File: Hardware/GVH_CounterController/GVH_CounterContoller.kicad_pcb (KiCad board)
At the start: 2 copper layers, 82.5 x 88.9 mm, 67 parts, among them J1 Molex Micro-Fit 5pos, J10 Molex Micro-Fit 2pos, J11 Molex Micro-Fit 3pos, J2 Conn_02x08_Odd_Even, J3 Molex Ultra-Fit, J6 Molex Micro-Fit 5pos, J7 WIZnet_J1B1211CCD_RJ45, J8 Molex Micro-Fit 2pos, J9 Molex Micro-Fit 2pos, K1 Relay_DPDT, Q1 MBT2222, SW2 SW_DIP_x02, SW3 SW_MEC_5G, U10 AO4882, U11 DS18B20_, U2 SN74LVC2T45, U3 Teensy4.1, U4 R-78E5.0-1.0, U5 SN74LVC2T45DCUR, U6 RT9080-3.3, U7 SN74LVC2T45DCUR, U8 SN74LVC2T45DCUR, U9 SN74LVC2G17

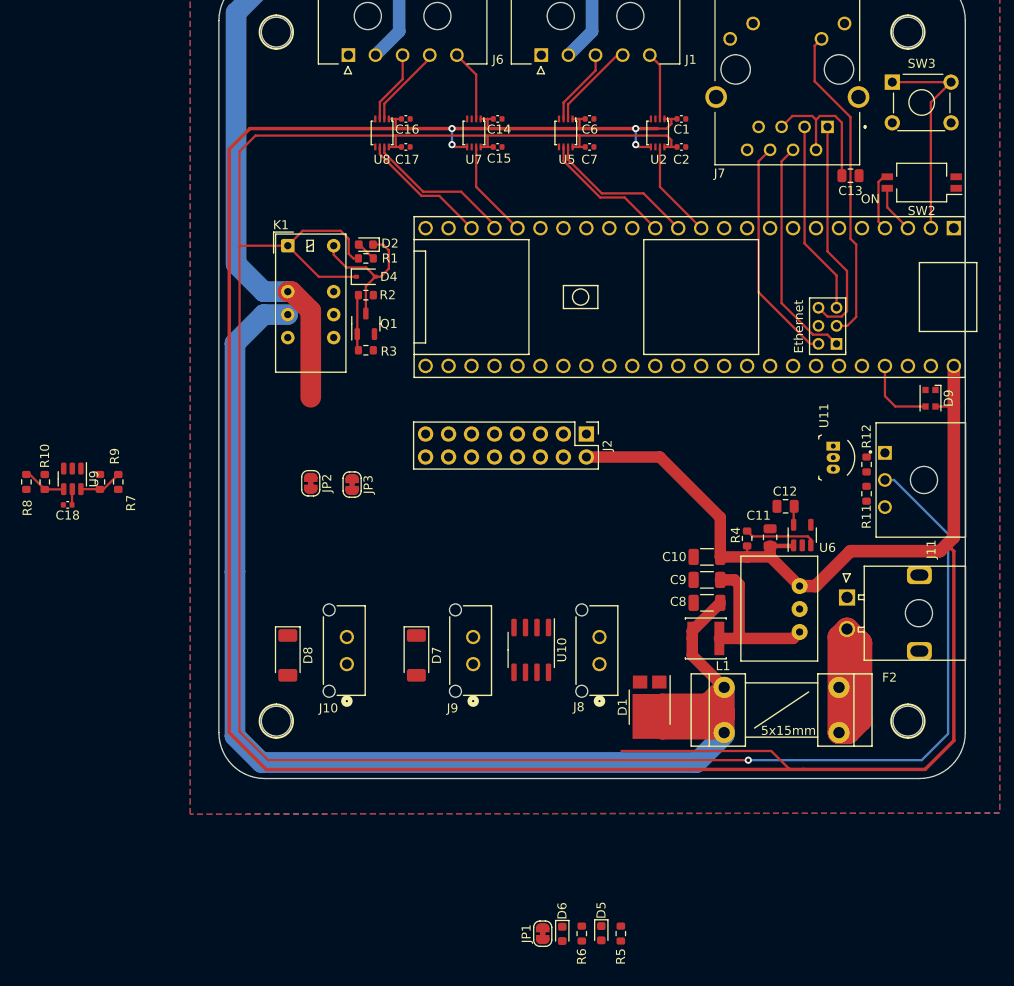
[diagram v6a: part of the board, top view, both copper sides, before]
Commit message: About to change gate driver buffer, it wont shift logic up
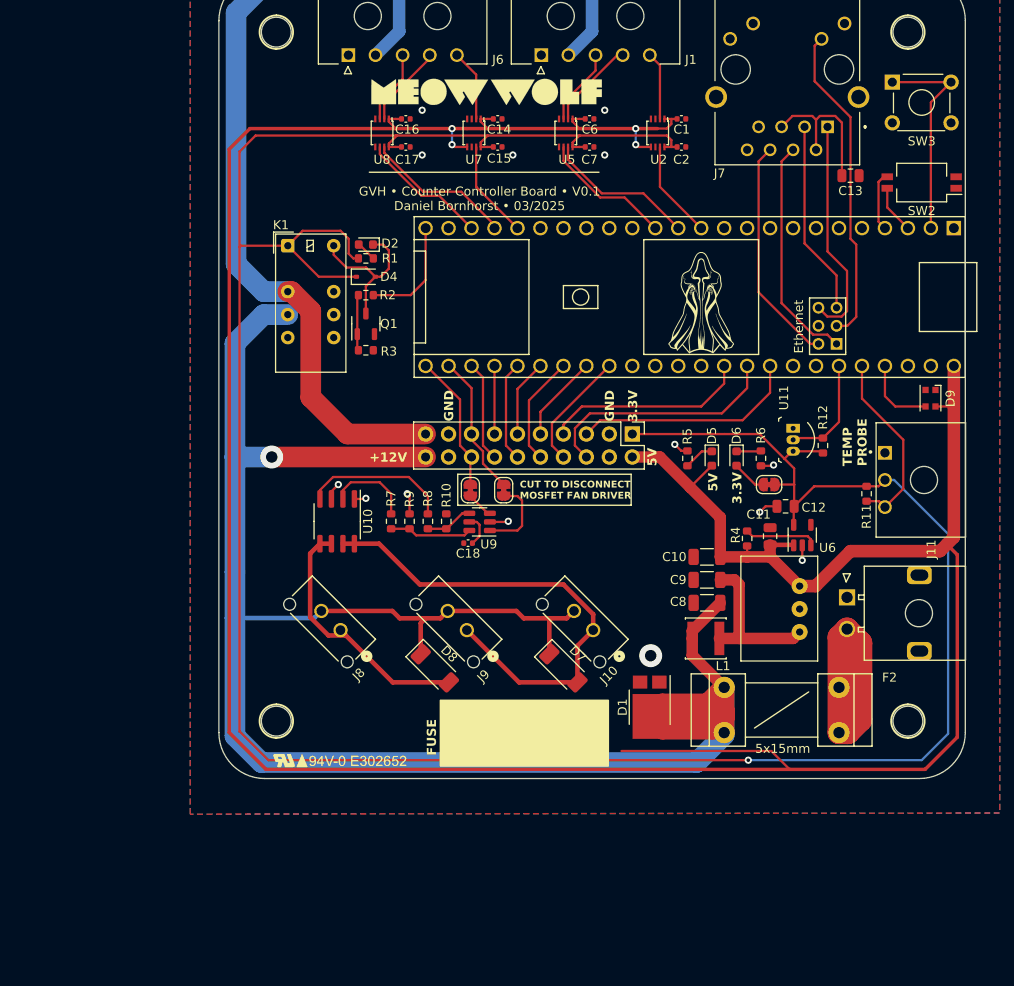
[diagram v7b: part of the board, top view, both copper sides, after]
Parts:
- removed J2: Conn_02x08_Odd_Even, Connector_PinHeader_2.54mm:PinHeader_2x08_P2.54mm_Vertical
- added G***: LOGO, 0_logo:UL_Mark_15mm, F.Cu at (89.5, 137.5)
- added G***: LOGO, 0_logo:MW_Logo_Horizontal_1.0inch, F.Cu at (105.8, 63.8)
- added J5: Conn_02x10_Odd_Even, Connector_PinHeader_2.54mm:PinHeader_2x10_P2.54mm_Vertical, F.Cu at (121.9, 101.6)
- added REF**: GVH_Cloak_Figure, 0_logo:GVH_Cloak_Figure, F.Cu at (129.6, 87.3)
- moved R6 56.2 mm to (136.1, 104.3), turned to -90 degrees
- moved D6 56.0 mm to (133.4, 104.3)
- moved JP1 55.6 mm to (137.0, 107.2), turned to 180 degrees
- moved D5 53.9 mm to (130.7, 104.3)
- moved R5 53.1 mm to (128.0, 104.3)
- moved U9 45.3 mm to (105.0, 111.3), turned to 180 degrees
- moved R10 44.6 mm to (101.3, 111.3)
- moved R8 44.6 mm to (99.3, 111.3), turned to 90 degrees
- moved C18 44.5 mm to (103.8, 113.7)
- moved R9 34.5 mm to (97.3, 111.3)
- moved R7 30.5 mm to (95.2, 111.3), turned to 90 degrees
- moved U10 25.7 mm to (89.3, 111.3)
- moved JP2 21.3 mm to (107.7, 107.8), turned to 90 degrees
- moved D7 16.3 mm to (114.3, 127.5), turned to -45 degrees
- moved D8 16.3 mm to (100.1, 127.5), turned to -45 degrees
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- renumbered J8 to J10, J10 to J8
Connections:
- D7 pad 2: FAN_DRAIN_1 -> FAN_DRAIN_0
- D8 pad 2: FAN_DRAIN_0 -> FAN_DRAIN_1
- J10 pad 1: FAN_DRAIN_1 -> FAN_DRAIN_0
- J8 pad 1: FAN_DRAIN_0 -> FAN_DRAIN_1
- JP2 pad 2: Net-(JP2-B) -> GPIO_11
- JP3 pad 2: Net-(JP3-B) -> GPIO_12
- U3 pad 24: unconnected-(U3-32_OUT1B-Pad24) -> TOUCH_RESET
- U3 pad 25: unconnected-(U3-33_MCLK2-Pad25) -> GPIO_12
- U3 pad 26: unconnected-(U3-34_RX8-Pad26) -> GPIO_11
- U3 pad 27: unconnected-(U3-35_TX8-Pad27) -> GPIO_10
- U3 pad 28: unconnected-(U3-36_CS-Pad28) -> GPIO_9
- U3 pad 29: unconnected-(U3-37_CS-Pad29) -> GPIO_8
- U3 pad 30: unconnected-(U3-38_CS1_IN1-Pad30) -> GPIO_7
- U3 pad 31: unconnected-(U3-39_MISO1_OUT1A-Pad31) -> GPIO_6
- U3 pad 32: unconnected-(U3-40_A16-Pad32) -> GPIO_5
- U3 pad 33: unconnected-(U3-41_A17-Pad33) -> GPIO_4
- U3 pad 38: unconnected-(U3-16_A2_RX4_SCL1-Pad38) -> GPIO_3
- U3 pad 39: unconnected-(U3-17_A3_TX4_SDA1-Pad39) -> GPIO_2
- U3 pad 40: unconnected-(U3-18_A4_SDA-Pad40) -> GPIO_1
- U3 pad 43: unconnected-(U3-21_A7_RX5_BCLK1-Pad43) -> TEMP_SENS_0
- U3 pad 44: unconnected-(U3-22_A8_CTX1-Pad44) -> TEMP_SENS_1
- U9 pad 1: Net-(JP2-B) -> FAN_CTRL_0
- U9 pad 3: Net-(JP3-B) -> FAN_CTRL_1
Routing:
- net +12V: track 158.2 -> 226.5 mm, vias 0 -> 1
- net FAN_DRAIN_0: track 0.00 -> 53.8 mm
- net +3.3V: track 262.6 -> 305.3 mm
- net FAN_DRAIN_1: track 0.00 -> 29.0 mm
- net GPIO_2: track 0.00 -> 27.0 mm
- net GPIO_1: track 0.00 -> 25.2 mm
- net GPIO_3: track 0.00 -> 22.6 mm
- net TEMP_SENS_1: track 0.00 -> 20.6 mm
- net Net-(R8-Pad2): track 0.00 -> 16.4 mm
- net GPIO_11: track 0.00 -> 15.7 mm
- net GPIO_12: track 0.00 -> 15.3 mm
- net GND: track 0.00 -> 14.5 mm, vias 0 -> 13
- net +12V_ISO: track 105.1 -> 119.4 mm
- net GPIO_4: track 0.00 -> 13.2 mm
- net TOUCH_RESET: track 0.00 -> 12.2 mm
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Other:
- board text added: "+12V"
- board text added: "3.3V"
- board text added: "5V"
- board text added: "CUT TO DISCONNECT MOSFET FAN DRIVER"
- board text added: "FUSE"
- board text added: "GND"
- board text added: "GVH • Counter Controller Board • V0.1 Daniel Bornhorst • 03/2025"
- board text added: "TEMP PROBE"
- board text removed: "ON"

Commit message: Controller board finished and documentation created
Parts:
- removed C18: 0.1uF, Capacitor_SMD:C_0402_1005Metric
- removed the U9 at (105.0, 111.3)
- added C13: 0.1uF, Capacitor_SMD:C_0402_1005Metric, F.Cu at (107.3, 111.0)
- added C14: 0.1uF, Capacitor_SMD:C_0402_1005Metric, F.Cu at (107.3, 114.3)
- added G***: LOGO, 0_logo:MW_Mark_0.50inch, B.Cu at (88.8, 68.8)
- added R1: 68R, Resistor_SMD:R_0402_1005Metric, F.Cu at (115.1, 65.0)
- added R13: 68R, Resistor_SMD:R_0402_1005Metric, F.Cu at (94.7, 65.0)
- added R14: 68R, Resistor_SMD:R_0402_1005Metric, F.Cu at (93.7, 65.0)
- added R2: 68R, Resistor_SMD:R_0402_1005Metric, F.Cu at (114.0, 65.0)
- added REF**: GVH_Cloak_Figure, 0_logo:GVH_Cloak_Figure, B.Cu at (132.0, 121.5)
- added U7: SN74LVC2T45DCUR, Package_SO:VSSOP-8_2.4x2.1mm_P0.5mm, F.Cu at (104.8, 112.6)
- J2: renamed from J5; value Conn_02x10_Odd_Even -> Vertical Header Pins
- J4: renamed from J9; value Molex Micro-Fit 2pos -> Molex Micro-Fit
- J5: renamed from J1; value Molex Micro-Fit 5pos -> Molex Micro-Fit
- J6: renamed from J10; value Molex Micro-Fit 2pos -> Molex Micro-Fit
- J7: renamed from J8; value Molex Micro-Fit 2pos -> Molex Micro-Fit
- J8: renamed from J6; value Molex Micro-Fit 5pos -> Molex Micro-Fit
- J9: renamed from J11; value Molex Micro-Fit 3pos -> Molex Micro-Fit
- U2: value SN74LVC2T45 -> SN74LVC2T45DCUR
- moved G*** 14.0 mm to (97.5, 75.1)
- moved R15 6.08 mm to (144.9, 102.9), turned to -90 degrees
- moved R10 1.40 mm to (99.3, 112.6)
- moved R11 1.40 mm to (97.3, 112.6)
- moved R12 1.40 mm to (101.3, 112.6)
- moved R9 1.40 mm to (95.2, 112.6)
- moved JP1 1.14 mm to (106.6, 107.8)
- moved REF** 0.72 mm to (129.6, 86.5)
- renumbered C12 to C10, C14 to C11, C15 to C12, C16 to C15, C17 to C16, C8 to C3, C9 to C4, C10 to C5, C13 to C8, C11 to C9, D4 to D3, D5 to D4, D6 to D5, D7 to D6, D8 to D7, D9 to D8, F2 to F1, J3 to J1, J7 to J3, JP2 to JP1, JP3 to JP2, JP1 to JP3, R8 to R10, R9 to R11, R10 to R12, R11 to R15, R12 to R16, R1 to R3, R2 to R5, R3 to R6, R5 to R7, R6 to R8, R7 to R9, SW2 to SW1, SW3 to SW2, U3 to U1, U11 to U10, U4 to U3, U5 to U4, U6 to U5, U7 to U6, U10 to U8, U8 to U9
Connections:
- U4 pad 2: LD_OUT_0 -> Net-(U4-A1)
- U4 pad 3: CLK_OUT_0 -> Net-(U4-A2)
- U9 pad 2: LD_OUT_1 -> Net-(U9-A1)
- U9 pad 3: CLK_OUT_1 -> Net-(U9-A2)
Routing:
- net GND: track 14.5 -> 85.8 mm, vias 13 -> 35
- net +3.3V: track 305.3 -> 332.9 mm
- net FAN_CTRL_0: track 8.80 -> 3.27 mm
- net TEMP_SENS_1: track 20.6 -> 23.7 mm
- net Net-(U7-B1): track 9.17 -> 12.0 mm
- net LD_OUT_1: track 9.14 -> 6.80 mm
- net CLK_OUT_1: track 8.10 -> 5.98 mm
- net CLK_OUT_0: track 8.52 -> 6.40 mm
- net LD_OUT_0: track 9.90 -> 7.86 mm
- net +5V: track 336.7 -> 335.0 mm
- net Net-(U7-B2): track 5.29 -> 6.71 mm
- net Net-(R9-Pad2): track 9.42 -> 10.8 mm
- net Net-(R10-Pad2): track 16.4 -> 17.8 mm
- net Net-(U9-A2): track 0.00 -> 1.33 mm
- net Net-(U4-A2): track 0.00 -> 1.33 mm
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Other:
- board text added: "12V"
- board text added: "1WIRE"
- board text added: "CLK"
- board text added: "LD"
- board text added: "SER"
